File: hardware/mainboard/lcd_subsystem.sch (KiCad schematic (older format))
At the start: 10 parts, among them J2 WP7B-S040VA1-R6000, U1 TPS65132

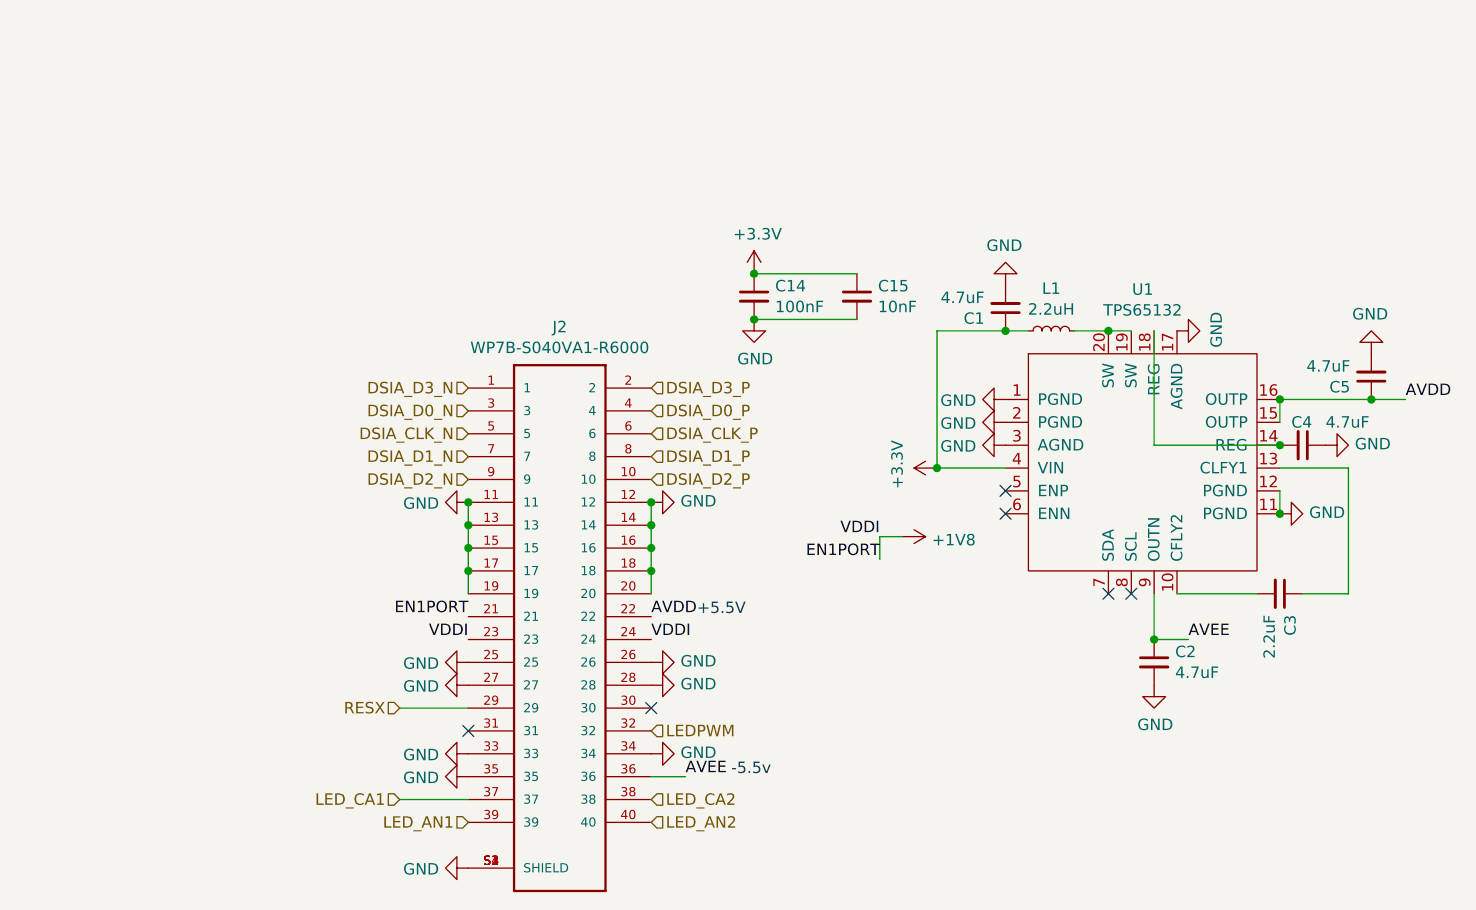
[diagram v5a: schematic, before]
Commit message: 3d models, 1v2 regulator footprint change
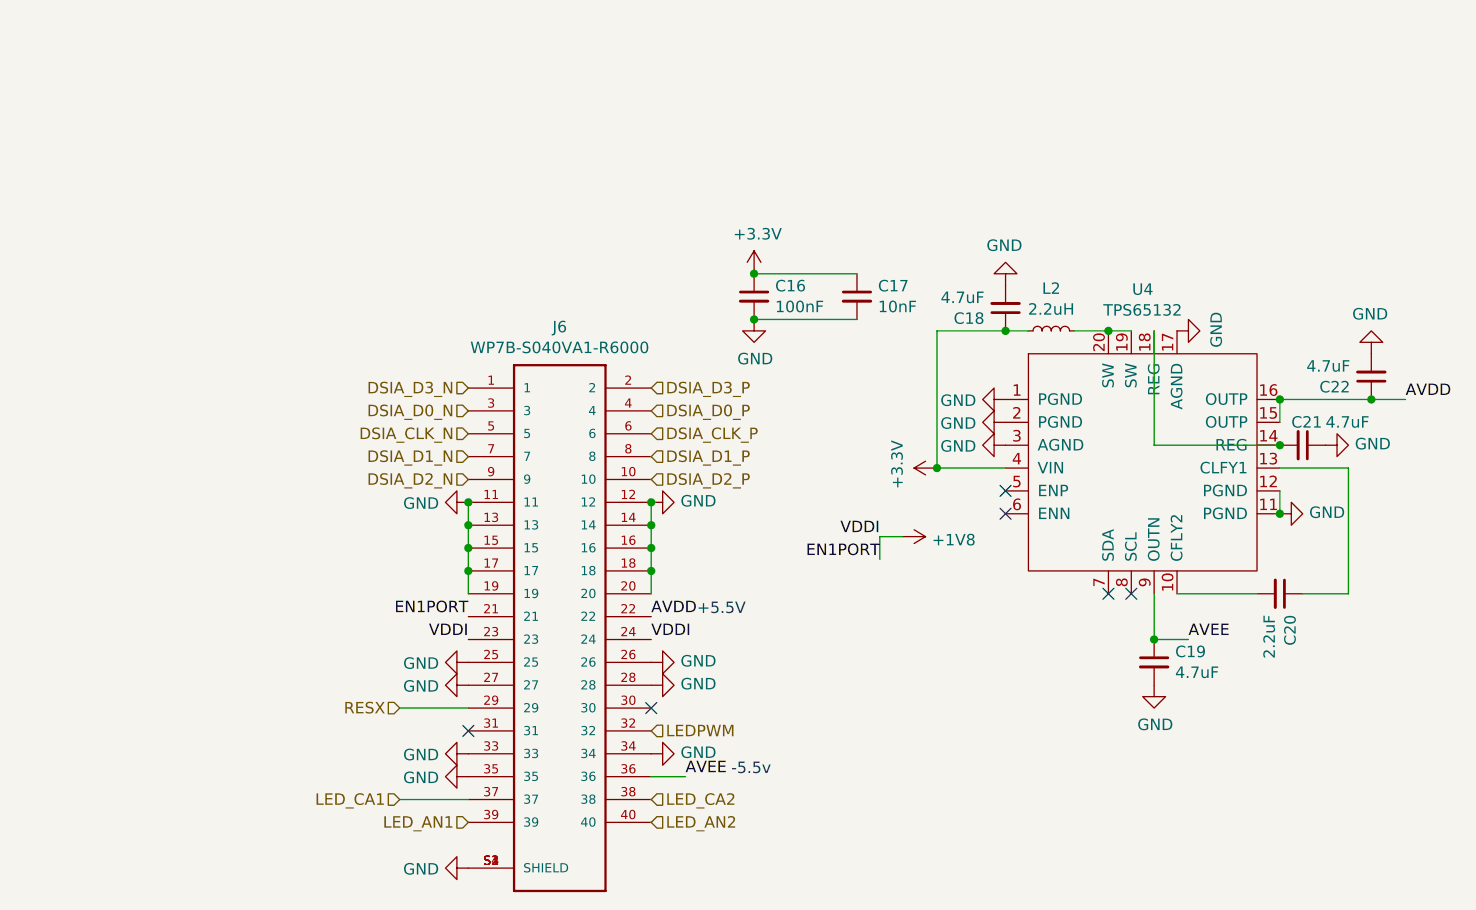
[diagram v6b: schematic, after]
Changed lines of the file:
@@
 $Descr A4 11693 8268
 encoding utf-8
-Sheet 2 3
+Sheet 3 3
 Title ""
 Date ""
@@
 AR Path="/5FA3B5FC/5FA221C8" Ref="J?"  Part="1"
 AR Path="/5FA75E62/5FA221C8" Ref="J6"  Part="1"
-F 0 "J2" H 4750 5717 50  0000 C CNN
+F 0 "J6" H 4750 5717 50  0000 C CNN
 F 1 "WP7B-S040VA1-R6000" H 4750 5626 50  0000 C CNN
 F 2 "mainboard:JAE_WP7B-S040VA1-R6000" H 4750 4450 50  0001 L BNN
@@
 AR Path="/5FA3B5FC/5F8F28BE" Ref="C?"  Part="1"
 AR Path="/5FA75E62/5F8F28BE" Ref="C19"  Part="1"
-F 0 "C2" H 7442 4696 50  0000 L CNN
+F 0 "C19" H 7442 4696 50  0000 L CNN
 F 1 "4.7uF" H 7442 4605 50  0000 L CNN
 F 2 "Capacitor_SMD:C_0402_1005Metric_Pad0.74x0.62mm_HandSolder" H 7350 4650 50  0001 C CNN
@@
 AR Path="/5FA3B5FC/5F8D1308" Ref="C?"  Part="1"
 AR Path="/5FA75E62/5F8D1308" Ref="C22"  Part="1"
-F 0 "C5" H 8392 3446 50  0000 L CNN
+F 0 "C22" H 8392 3446 50  0000 L CNN
 F 1 "4.7uF" H 8392 3355 50  0000 L CNN
 F 2 "Capacitor_SMD:C_0402_1005Metric_Pad0.74x0.62mm_HandSolder" H 8300 3400 50  0001 C CNN
@@
 AR Path="/5FA3B5FC/5F8FE2CF" Ref="C?"  Part="1"
 AR Path="/5FA75E62/5F8FE2CF" Ref="C21"  Part="1"
-F 0 "C4" V 7900 3650 50  0000 L CNN
+F 0 "C21" V 7900 3650 50  0000 L CNN
 F 1 "4.7uF" V 7900 3800 50  0000 L CNN
 F 2 "Capacitor_SMD:C_0402_1005Metric_Pad0.74x0.62mm_HandSolder" H 8000 3700 50  0001 C CNN
@@
 AR Path="/5FA3B5FC/5F901A08" Ref="C?"  Part="1"
 AR Path="/5FA75E62/5F901A08" Ref="C20"  Part="1"
-F 0 "C3" H 7992 4396 50  0000 L CNN
+F 0 "C20" H 7992 4396 50  0000 L CNN
 F 1 "2.2uF" H 7992 4305 50  0000 L CNN
 F 2 "Capacitor_SMD:C_0402_1005Metric_Pad0.74x0.62mm_HandSolder" H 7900 4350 50  0001 C CNN
@@
 AR Path="/5FA3B5FC/5F908EBB" Ref="L?"  Part="1"
 AR Path="/5FA75E62/5F908EBB" Ref="L2"  Part="1"
-F 0 "L1" V 7085 3200 50  0000 C CNN
+F 0 "L2" V 7085 3200 50  0000 C CNN
 F 1 "2.2uH" V 6994 3200 50  0000 C CNN
 F 2 "Inductor_SMD:L_0805_2012Metric_Pad1.15x1.40mm_HandSolder" H 6900 3200 50  0001 C CNN
@@
 AR Path="/5FA3B5FC/5F90F3A3" Ref="C?"  Part="1"
 AR Path="/5FA75E62/5F90F3A3" Ref="C18"  Part="1"
-F 0 "C1" H 6792 3146 50  0000 L CNN
+F 0 "C18" H 6792 3146 50  0000 L CNN
 F 1 "4.7uF" H 6792 3055 50  0000 L CNN
 F 2 "Capacitor_SMD:C_0402_1005Metric_Pad0.74x0.62mm_HandSolder" H 6700 3100 50  0001 C CNN
@@
 AR Path="/5FA3B5FC/5F8CA6D9" Ref="U?"  Part="1"
 AR Path="/5FA75E62/5F8CA6D9" Ref="U4"  Part="1"
-F 0 "U1" H 7300 4381 50  0000 C CNN
+F 0 "U4" H 7300 4381 50  0000 C CNN
 F 1 "TPS65132" H 7300 4290 50  0000 C CNN
 F 2 "mainboard:TPS65132WRVCT" H 7300 3650 50  0001 C CNN
@@
 AR Path="/5F86493C/6021F152" Ref="C14"  Part="1"
 AR Path="/5FA75E62/6021F152" Ref="C16"  Part="1"
-F 0 "C14" H 5692 3096 50  0000 L CNN
+F 0 "C16" H 5692 3096 50  0000 L CNN
 F 1 "100nF" H 5692 3005 50  0000 L CNN
 F 2 "Capacitor_SMD:C_0402_1005Metric_Pad0.74x0.62mm_HandSolder" H 5600 3050 50  0001 C CNN
@@
 AR Path="/5F86493C/602249E9" Ref="C15"  Part="1"
 AR Path="/5FA75E62/602249E9" Ref="C17"  Part="1"
-F 0 "C15" H 6142 3096 50  0000 L CNN
+F 0 "C17" H 6142 3096 50  0000 L CNN
 F 1 "10nF" H 6142 3005 50  0000 L CNN
 F 2 "Capacitor_SMD:C_0402_1005Metric_Pad0.74x0.62mm_HandSolder" H 6050 3050 50  0001 C CNN

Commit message: redesign started, symbol scripts, new dsi chip
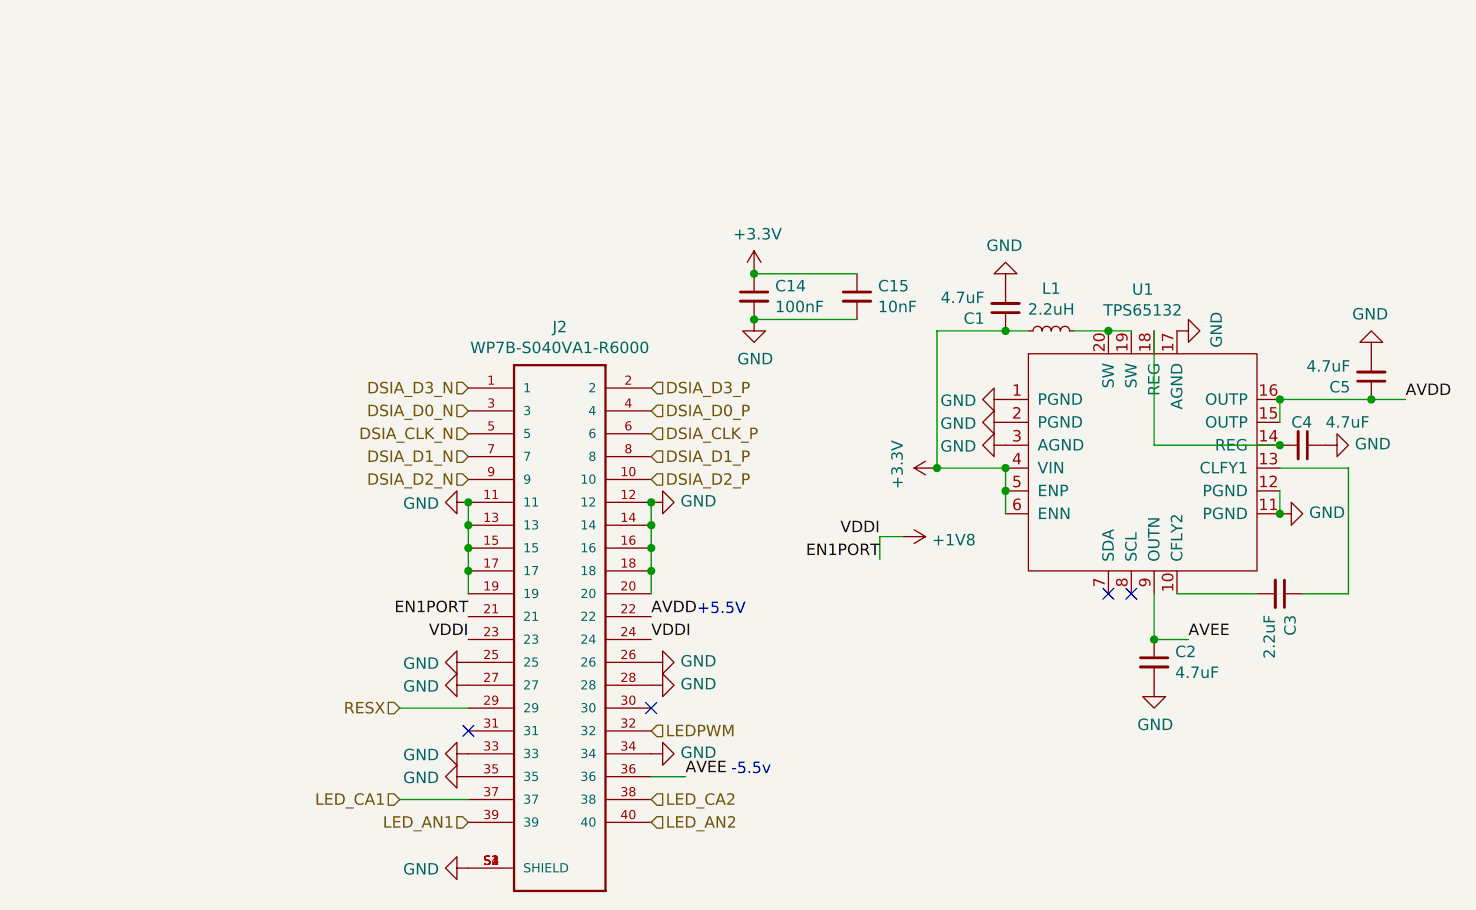
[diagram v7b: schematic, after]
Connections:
- net +3V3: now also U1.5 (ENP), U1.6 (ENN)
- no-connect marks 6 -> 4

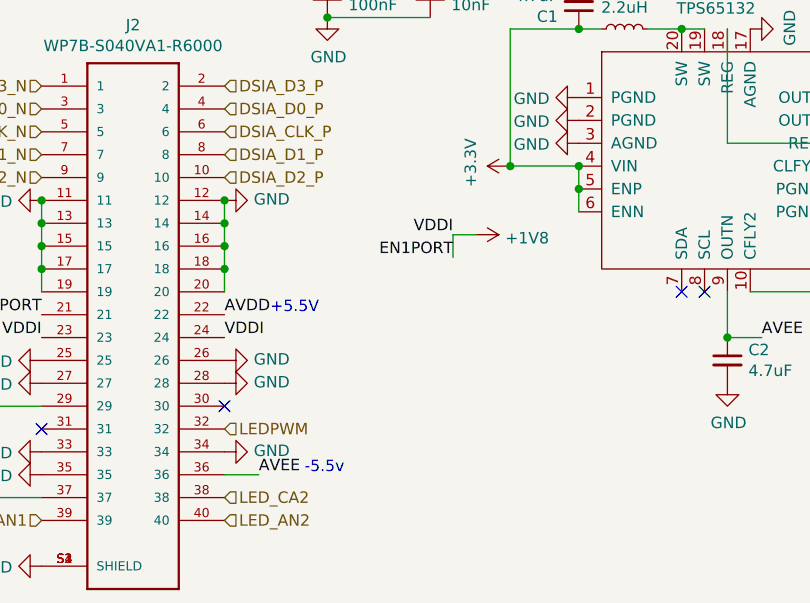
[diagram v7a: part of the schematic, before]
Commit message: finish sch arch, remove coproc, add bl driver, need to do TC power supply
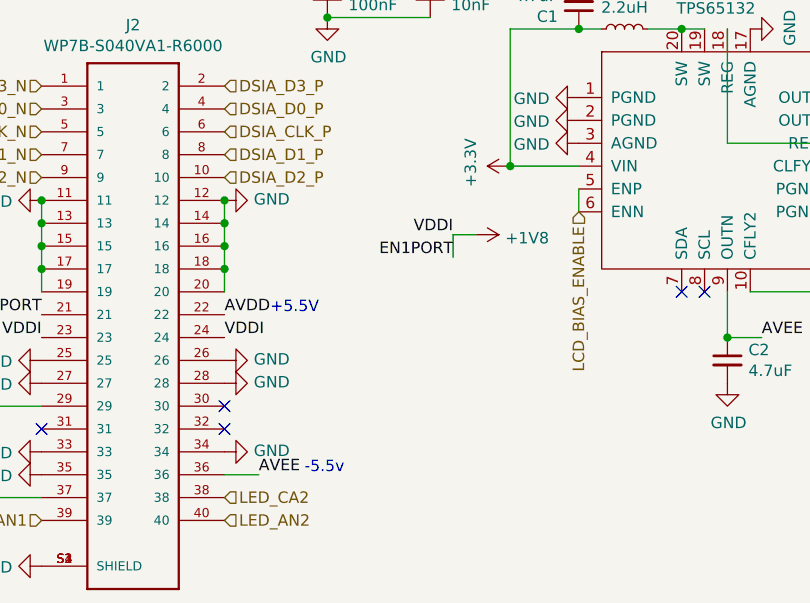
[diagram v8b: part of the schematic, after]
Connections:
- net +3V3: no longer U1.5 (ENP), U1.6 (ENN)
- net LEDPWM: no longer names the net of J2.32
- new net LCD_BIAS_ENABLE: U1.5 (ENP), U1.6 (ENN)
- no-connect marks 4 -> 5
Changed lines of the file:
@@
 Text HLabel 5150 5350 2    50   Input ~ 0
 LED_AN2
-Text HLabel 5150 4950 2    50   Input ~ 0
-LEDPWM
 $Comp
 L Device:C_Small C14
@@
 Wire Wire Line
 	6700 4000 6700 3900
-Connection ~ 6700 3800
-Connection ~ 6700 3900
-Wire Wire Line
-	6700 3900 6700 3800
+Text HLabel 6700 4000 3    50   Input ~ 0
+LCD_BIAS_ENABLE
+NoConn ~ 5150 4950
 $EndSCHEMATC
